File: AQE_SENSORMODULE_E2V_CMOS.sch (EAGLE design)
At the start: 35 parts, among them J1 440055-4, J2 AVR_SPI_PRG_6NS, U1 V_REG_LDOSMD, U2 V_REG_LDOSMD, U3 MCP41XXX

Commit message: updated files
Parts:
- C1, C2, C3, C5, C6, C8: device SparkFun:CAP0603-CAP -> SparkFun-Passives:CAP0805
- R11: value 470ohm -> 270ohm
- R5: value (none) -> 10R
- renumbered U$4 to GAS
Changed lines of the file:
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@@
 <part name="SUPPLY3" library="supply2" deviceset="GND" device=""/>
 <part name="P+3" library="SparkFun" deviceset="VCC" device=""/>
-<part name="C3" library="SparkFun" deviceset="CAP" device="0603-CAP" value="0.1uF"/>
+<part name="C3" library="SparkFun-Passives" deviceset="CAP" device="0805" value="0.1uF"/>
 <part name="C4" library="wicked-device" deviceset="EEE-1EA100WR" device="" value="10uF"/>
-<part name="U$4" library="ricardo" deviceset="E2V" device=""/>
+<part name="GAS" library="ricardo" deviceset="E2V" device=""/>
 <part name="R1" library="SparkFun" deviceset="RESISTOR" device="0805-RES"/>
 <part name="U$5" library="SparkFun" deviceset="1.8V" device="" value="SENSOR_VCC"/>
@@
 <part name="P+5" library="SparkFun" deviceset="VCC" device=""/>
 <part name="SUPPLY6" library="supply2" deviceset="GND" device=""/>
-<part name="C5" library="SparkFun" deviceset="CAP" device="0603-CAP" value="0.1uF"/>
+<part name="C5" library="SparkFun-Passives" deviceset="CAP" device="0805" value="0.1uF"/>
 <part name="MAC" library="nanode" deviceset="11AA02E48" device=""/>
 <part name="SUPPLY7" library="supply2" deviceset="GND" device=""/>
 <part name="P+6" library="SparkFun" deviceset="VCC" device=""/>
-<part name="C6" library="SparkFun" deviceset="CAP" device="0603-CAP" value="0.1uF"/>
+<part name="C6" library="SparkFun-Passives" deviceset="CAP" device="0805" value="0.1uF"/>
 <part name="R4" library="SparkFun" deviceset="RESISTOR" device="0805-RES" value="2.4MOhm"/>
 <part name="U1" library="SparkFun" deviceset="V_REG_LDO" device="SMD"/>
@@
 <part name="P+7" library="SparkFun" deviceset="VCC" device=""/>
 <part name="HEATER_VCC1" library="SparkFun" deviceset="1.8V" device="" value="SENSOR_VCC"/>
-<part name="C8" library="SparkFun" deviceset="CAP" device="0603-CAP" value="0.1uF"/>
+<part name="C8" library="SparkFun-Passives" deviceset="CAP" device="0805" value="0.1uF"/>
 <part name="C9" library="wicked-device" deviceset="EEE-1EA100WR" device="" value="10uF"/>
 <part name="R9" library="SparkFun" deviceset="RESISTOR" device="0805-RES" value="0Ohm"/>
@@
 <part name="R10" library="SparkFun" deviceset="RESISTOR" device="0805-RES" value="270ohm"/>
 <part name="PWR" library="adafruit" deviceset="LED" device="CHIPLED_0805" value="RED"/>
-<part name="R11" library="SparkFun" deviceset="RESISTOR" device="0805-RES" value="470ohm"/>
+<part name="R11" library="SparkFun" deviceset="RESISTOR" device="0805-RES" value="270ohm"/>
 <part name="MCU" library="axeio-SparkFun" deviceset="ATTINY48" device="32A"/>
 <part name="SUPPLY2" library="supply2" deviceset="GND" device=""/>
 <part name="P+2" library="SparkFun" deviceset="VCC" device=""/>
-<part name="C1" library="SparkFun" deviceset="CAP" device="0603-CAP" value="0.1uF"/>
-<part name="R5" library="SparkFun" deviceset="RESISTOR" device="0805-RES"/>
+<part name="C1" library="SparkFun-Passives" deviceset="CAP" device="0805" value="0.1uF"/>
+<part name="R5" library="SparkFun" deviceset="RESISTOR" device="0805-RES" value="10R"/>
 <part name="U3" library="SparkFun-AnalogIC" deviceset="MCP41XXX" device=""/>
-<part name="C2" library="SparkFun" deviceset="CAP" device="0603-CAP" value="0.1uF"/>
+<part name="C2" library="SparkFun-Passives" deviceset="CAP" device="0805" value="0.1uF"/>
 <part name="SUPPLY8" library="supply2" deviceset="GND" device=""/>
 <part name="P+9" library="SparkFun" deviceset="VCC" device=""/>
@@
 <attribute name="NAME" x="124.714" y="202.311" size="1.778" layer="95"/>
 </instance>
-<instance part="U$4" gate="G$1" x="62.23" y="76.2" rot="R180"/>
+<instance part="GAS" gate="G$1" x="62.23" y="76.2" rot="R180"/>
 <instance part="R1" gate="G$1" x="104.14" y="66.04" rot="R90"/>
 <instance part="U$5" gate="G$1" x="125.73" y="87.63" smashed="yes">
@@
 </segment>
 <segment>
-<pinref part="U$4" gate="G$1" pin="VHEATER+"/>
+<pinref part="GAS" gate="G$1" pin="VHEATER+"/>
 <wire x1="82.55" y1="81.28" x2="120.65" y2="81.28" width="0.1524" layer="91"/>
 <label x="120.65" y="81.28" size="1.778" layer="95" xref="yes"/>
@@
 <net name="SENSOR_VCC" class="0">
 <segment>
-<pinref part="U$4" gate="G$1" pin="VSENS+"/>
+<pinref part="GAS" gate="G$1" pin="VSENS+"/>
 <wire x1="82.55" y1="86.36" x2="125.73" y2="86.36" width="0.1524" layer="91"/>
 <pinref part="U$5" gate="G$1" pin="1.8V"/>
@@
 <net name="SENSOR" class="0">
 <segment>
-<label x="293.37" y="205.74" size="1.778" layer="95" xref="yes"/>
+<label x="278.13" y="205.74" size="1.778" layer="95" xref="yes"/>
 <pinref part="MCU" gate="G$1" pin="PC0(ADC0/PCINT8)"/>
-<wire x1="293.37" y1="205.74" x2="271.78" y2="205.74" width="0.1524" layer="91"/>
-</segment>
-<segment>
-<pinref part="U$4" gate="G$1" pin="VSENS-"/>
+<wire x1="278.13" y1="205.74" x2="271.78" y2="205.74" width="0.1524" layer="91"/>
+</segment>
+<segment>
+<pinref part="GAS" gate="G$1" pin="VSENS-"/>
 <wire x1="121.285" y1="76.2" x2="104.14" y2="76.2" width="0.1524" layer="91"/>
 <label x="121.285" y="76.2" size="1.778" layer="95" xref="yes"/>
@@
 <net name="HEATER_FEEDBACK" class="0">
 <segment>
-<pinref part="U$4" gate="G$1" pin="GND_HEATER"/>
+<pinref part="GAS" gate="G$1" pin="GND_HEATER"/>
 <wire x1="82.55" y1="71.12" x2="86.36" y2="71.12" width="0.1524" layer="91"/>
 <pinref part="R5" gate="G$1" pin="2"/>
@@
 </segment>
 <segment>
-<wire x1="271.78" y1="203.2" x2="308.61" y2="203.2" width="0.1524" layer="91"/>
-<label x="308.61" y="203.2" size="1.778" layer="95" xref="yes"/>
+<wire x1="271.78" y1="203.2" x2="293.37" y2="203.2" width="0.1524" layer="91"/>
+<label x="293.37" y="203.2" size="1.778" layer="95" xref="yes"/>
 <pinref part="MCU" gate="G$1" pin="PC1(ADC1/PCINT9)"/>
 </segment>

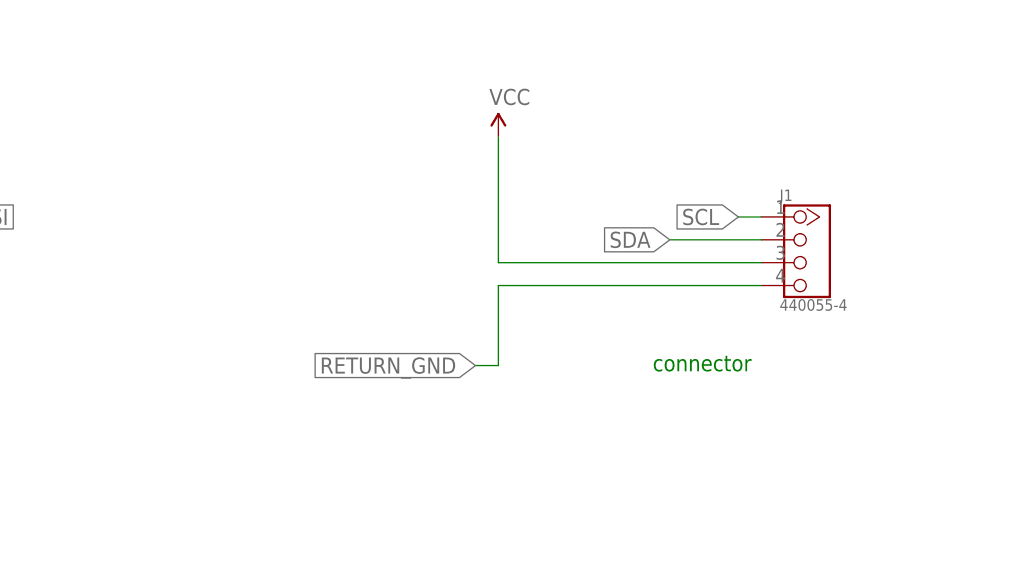
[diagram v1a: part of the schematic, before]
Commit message: flipped J1 connector pinout around by 180 degrees
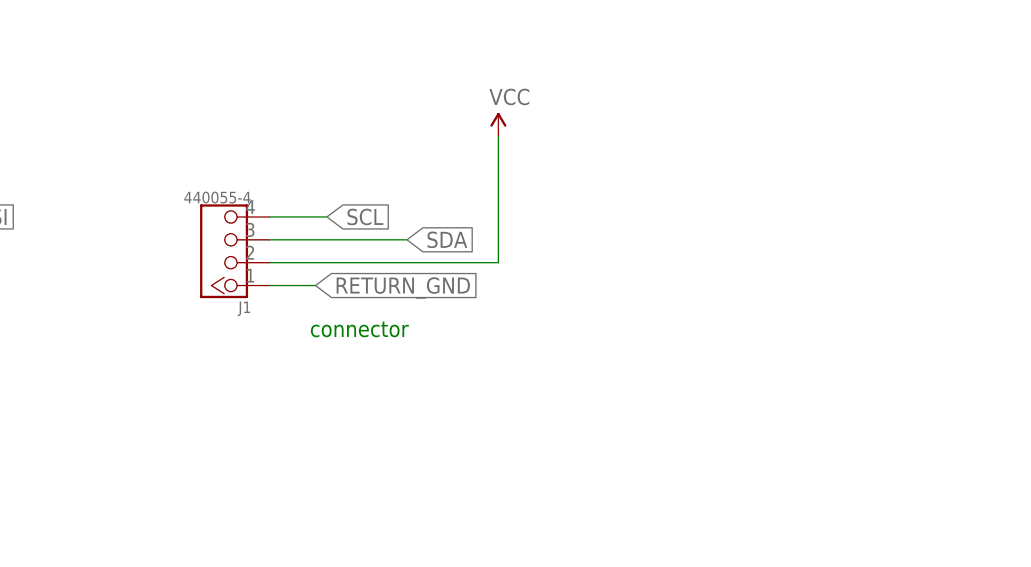
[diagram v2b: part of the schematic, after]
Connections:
- net RETURN_GND: now also J1.1; no longer J1.4
- net SCL: now also J1.4; no longer J1.1
- net SDA: now also J1.3; no longer J1.2
- net VCC: now also J1.2; no longer J1.3
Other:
- moved on the sheet: J1
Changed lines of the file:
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@@
 <setting verticaltext="up"/>
 </settings>
-<grid distance="0.1" unitdist="inch" unit="inch" style="lines" multiple="1" display="no" altdistance="0.01" altunitdist="inch" altunit="inch"/>
+<grid distance="0.05" unitdist="inch" unit="inch" style="lines" multiple="1" display="no" altdistance="0.01" altunitdist="inch" altunit="inch"/>
 <layers>
 <layer number="1" name="Top" color="4" fill="1" visible="no" active="no"/>
@@
 <text x="228.6" y="158.75" size="1.778" layer="91">microcontroller</text>
 <text x="64.135" y="60.325" size="1.778" layer="91">sensor</text>
-<text x="385.445" y="90.805" size="1.778" layer="91">connector</text>
+<text x="347.345" y="94.615" size="1.778" layer="91">connector</text>
 <wire x1="40.64" y1="266.7" x2="40.64" y2="7.62" width="0.1524" layer="94" style="shortdash"/>
 <wire x1="40.64" y1="7.62" x2="152.4" y2="7.62" width="0.1524" layer="94" style="shortdash"/>
@@
 <attribute name="VALUE" x="106.934" y="87.376" size="1.778" layer="96"/>
 </instance>
-<instance part="J1" gate="G$1" x="401.32" y="104.14"/>
+<instance part="J1" gate="G$1" x="339.09" y="104.14" rot="R180"/>
 <instance part="P+4" gate="1" x="368.3" y="116.84"/>
 <instance part="R6" gate="G$1" x="95.25" y="247.65"/>
@@
 </segment>
 <segment>
-<pinref part="J1" gate="G$1" pin="3"/>
 <pinref part="P+4" gate="1" pin="VCC"/>
-<wire x1="397.51" y1="102.87" x2="368.3" y2="102.87" width="0.1524" layer="91"/>
+<wire x1="342.9" y1="102.87" x2="368.3" y2="102.87" width="0.1524" layer="91"/>
 <wire x1="368.3" y1="102.87" x2="368.3" y2="116.84" width="0.1524" layer="91"/>
+<pinref part="J1" gate="G$1" pin="2"/>
 </segment>
 <segment>
@@
 </segment>
 <segment>
-<pinref part="J1" gate="G$1" pin="2"/>
-<wire x1="397.51" y1="105.41" x2="387.35" y2="105.41" width="0.1524" layer="91"/>
-<label x="387.35" y="105.41" size="1.778" layer="95" rot="R180" xref="yes"/>
+<wire x1="342.9" y1="105.41" x2="358.14" y2="105.41" width="0.1524" layer="91"/>
+<label x="358.14" y="105.41" size="1.778" layer="95" xref="yes"/>
+<pinref part="J1" gate="G$1" pin="3"/>
 </segment>
 </net>
@@
 </segment>
 <segment>
-<pinref part="J1" gate="G$1" pin="1"/>
-<wire x1="397.51" y1="107.95" x2="394.97" y2="107.95" width="0.1524" layer="91"/>
-<label x="394.97" y="107.95" size="1.778" layer="95" rot="R180" xref="yes"/>
+<label x="349.25" y="107.95" size="1.778" layer="95" xref="yes"/>
+<pinref part="J1" gate="G$1" pin="4"/>
+<wire x1="349.25" y1="107.95" x2="342.9" y2="107.95" width="0.1524" layer="91"/>
 </segment>
 </net>
@@
 <net name="RETURN_GND" class="0">
 <segment>
-<pinref part="J1" gate="G$1" pin="4"/>
-<wire x1="397.51" y1="100.33" x2="368.3" y2="100.33" width="0.1524" layer="91"/>
-<wire x1="368.3" y1="100.33" x2="368.3" y2="91.44" width="0.1524" layer="91"/>
-<wire x1="368.3" y1="91.44" x2="365.76" y2="91.44" width="0.1524" layer="91"/>
-<label x="365.76" y="91.44" size="1.778" layer="95" rot="R180" xref="yes"/>
-</segment>
-<segment>
+<wire x1="342.9" y1="100.33" x2="347.98" y2="100.33" width="0.1524" layer="91"/>
+<label x="347.98" y="100.33" size="1.778" layer="95" xref="yes"/>
+<pinref part="J1" gate="G$1" pin="1"/>
+</segment>
+<segment>
